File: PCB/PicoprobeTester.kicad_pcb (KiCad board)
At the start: 2 copper layers, 116.7 x 55.7 mm, 10 parts, among them J1 External_Connections

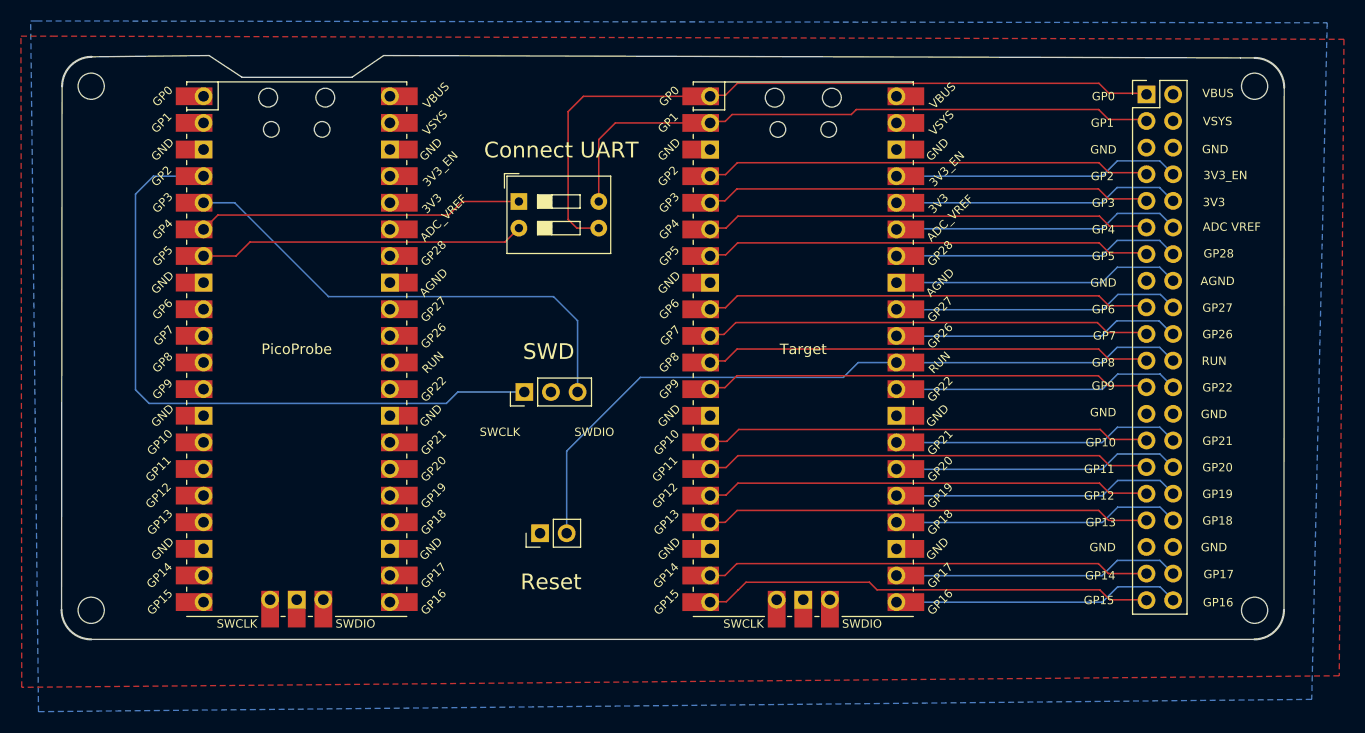
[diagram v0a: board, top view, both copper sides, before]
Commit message: Connected VBus and added text
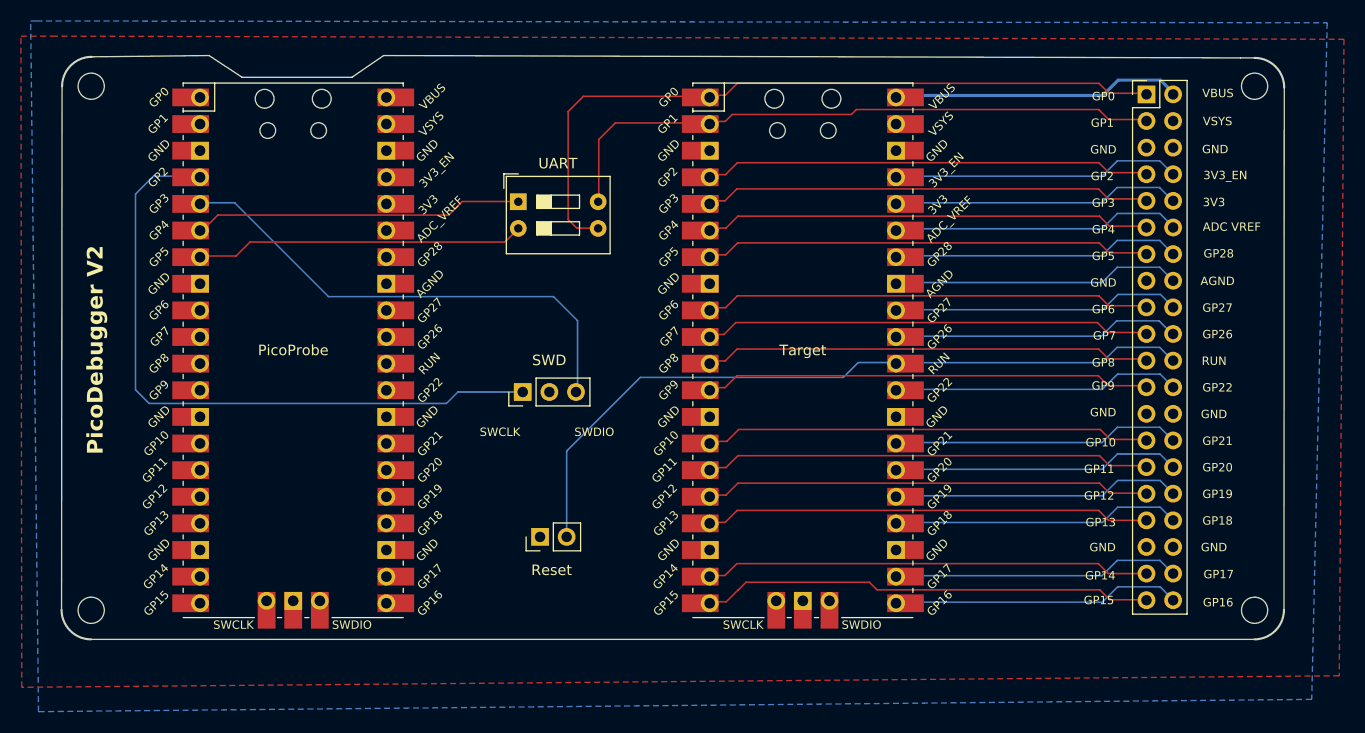
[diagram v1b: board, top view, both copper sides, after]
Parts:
- removed Connect UART: UART, Button_Switch_THT:SW_DIP_SPSTx02_Slide_9.78x7.26mm_W7.62mm_P2.54mm
- added UART: UART, Button_Switch_THT:SW_DIP_SPSTx02_Slide_9.78x7.26mm_W7.62mm_P2.54mm, F.Cu at (90.8, 83.0)
- moved PicoProbe 0.35 mm to (69.3, 97.2)
- moved Reset 0.35 mm to (92.8, 115.0)
- moved SWD 0.15 mm to (91.2, 101.2)
- moved Target 0.11 mm to (117.9, 97.2)
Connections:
- J1 pad 2: GND -> /VBus
- Target pad 40: unconnected-(Target1-VBUS-Pad40) -> /VBus
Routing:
- net /VBus: track 0.00 -> 27.5 mm
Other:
- board text added: "PicoDebugger V2"
